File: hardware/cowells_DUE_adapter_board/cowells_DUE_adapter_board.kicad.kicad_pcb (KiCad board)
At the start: 2 copper layers, 123.8 x 53.3 mm, 41 parts, among them J1 DRV8305J1, J2 DRV8305J2, J3 AS5048A, J4 spindl enc., J5 AS5311AB, J6 AS5311AB, SW1 Run, SW2 Dir, SW3 eStop, SW4 sw_rst, SW5 SW_DIP_x03, U1 NL17SZ14, Y1 20MHz

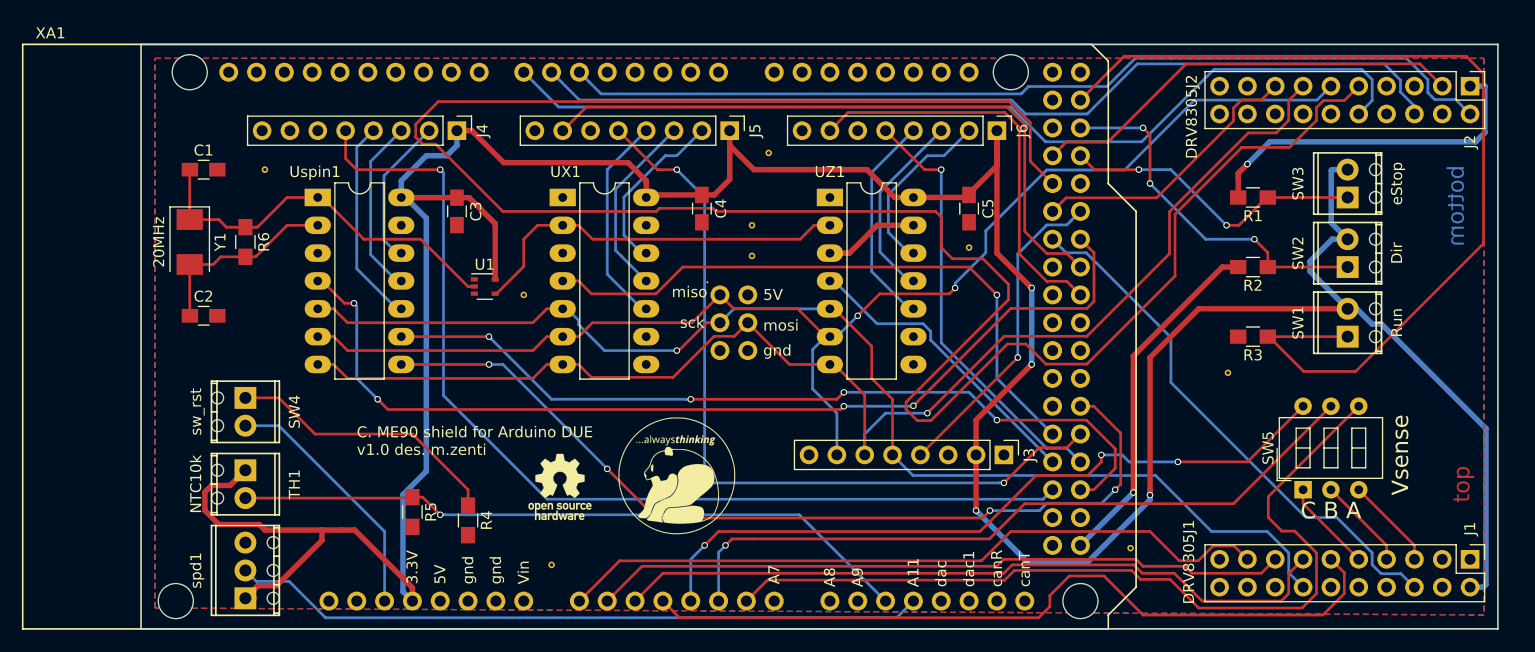
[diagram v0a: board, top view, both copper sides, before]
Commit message: cleanup of old code
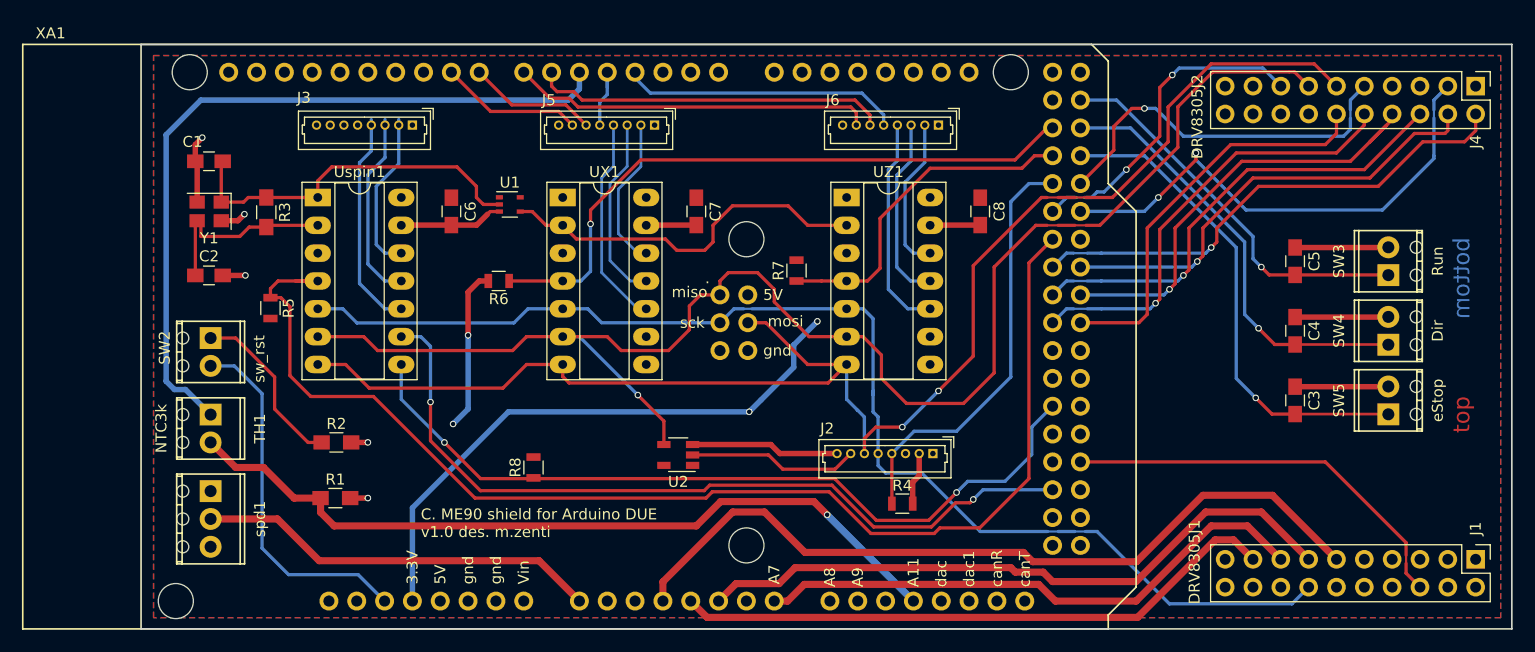
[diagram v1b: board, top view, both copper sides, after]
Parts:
- removed G***: LOGO, customSymbols:alwaysthinking_logo_10.8x10.8mm
- removed the J4 at (131.1, 70.1)
- removed the R1 at (203.7, 76.2)
- removed the R2 at (203.7, 82.5)
- removed the R3 at (203.7, 88.9)
- removed REF** (x9): stitching_VIA_0.6mm, customSymbols:stitching_VIA_0.6mm
- removed REF***: OSHW-Logo_5.7x6mm_SilkScreen, Symbols:OSHW-Logo_5.7x6mm_SilkScreen
- removed SW1: Run, TerminalBlocks_Phoenix:TerminalBlock_Phoenix_MPT-2.54mm_2pol
- removed the SW5 at (208.3, 102.9)
- added C3: 15n, Capacitors_SMD:C_0805_HandSoldering, F.Cu at (207.6, 94.7)
- added C4: 15n, Capacitors_SMD:C_0805_HandSoldering, F.Cu at (207.6, 88.4)
- added C5: 15n, Capacitors_SMD:C_0805_HandSoldering, F.Cu at (207.6, 82.0)
- added J2: AS5048A, Connectors_Molex:Molex_PicoBlade_53047-0810_08x1.25mm_Straight, F.Cu at (174.5, 99.6)
- added R4: 10k, Resistors_SMD:R_0805, F.Cu at (171.7, 104.1)
- added R5: 10k, Resistors_SMD:R_0805, F.Cu at (114.0, 86.3)
- added R6: 10k, Resistors_SMD:R_0805, F.Cu at (134.9, 83.8)
- added R7: 10k, Resistors_SMD:R_0805, F.Cu at (162.1, 82.9)
- added R8: 10k, Resistors_SMD:R_0805, F.Cu at (138.0, 100.8)
- added SW3: Run, TerminalBlocks_Phoenix:TerminalBlock_Phoenix_MPT-2.54mm_2pol, F.Cu at (216.1, 83.3)
- added U2: 74AHC1G125, TO_SOT_Packages_SMD:TSOT-23-5, F.Cu at (151.3, 99.7)
- C1, C2: value Cm -> 18p
- J3: value AS5048A -> spindl enc.; footprint Pin_Headers:Pin_Header_Straight_1x08_Pitch2.54mm -> Connectors_Molex:Molex_PicoBlade_53047-0810_08x1.25mm_Straight
- J5, J6: footprint Pin_Headers:Pin_Header_Straight_1x08_Pitch2.54mm -> Connectors_Molex:Molex_PicoBlade_53047-0810_08x1.25mm_Straight
- R1: renamed from R5; value 5k -> 1k
- TH1: value NTC10k -> NTC3k
- UX1, UZ1, Uspin1: footprint Housings_DIP:DIP-14_W7.62mm_LongPads -> Housings_DIP:DIP-14_W7.62mm_Socket_LongPads
- XA1: footprint Arduino:Arduino_Due_Shield_noHoles -> customFootPrints:Arduino_Due_Shield_drv8305
- Y1: value 20MHz -> 10MHz; footprint Crystals:Crystal_SMD_Abracon_ABM3-2pin_5.0x3.2mm -> Crystals:Crystal_SMD_3225-4pin_3.2x2.5mm
- spd1: value 0.3k -> 5k
- moved J3 61.8 mm to (127.0, 69.6), turned to 180 degrees
- moved SW5 20.1 mm to (216.1, 96.0)
- moved R2 14.0 mm to (120.1, 98.6), turned to 0 degrees
- moved spd1 10.3 mm to (108.6, 103.0), turned to 270 degrees
- moved SW4 8.00 mm to (216.1, 89.6)
- moved U1 7.83 mm to (135.9, 76.8)
- moved R1 7.15 mm to (120.0, 103.6), turned to 0 degrees
- moved J5 6.88 mm to (149.1, 69.6), turned to 180 degrees
- moved SW2 6.32 mm to (108.6, 89.0)
- moved TH1 5.99 mm to (108.6, 96.0)
- moved J6 5.36 mm to (175.0, 69.6), turned to 180 degrees
- moved C2 3.72 mm to (108.4, 83.3)
- moved R3 3.32 mm to (113.7, 77.5)
- moved Y1 3.31 mm to (108.5, 77.5), turned to 180 degrees
- moved UZ1 1.52 mm to (166.6, 76.2)
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- renumbered C3 to C6, C4 to C7, C5 to C8, J2 to J4, R4 to R2, R6 to R3, SW4 to SW2, SW2 to SW4, SW3 to SW5
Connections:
- J1 pad 14: /SCLK -> /SCK
- J1 pad 2: VCC -> Net-(J1-Pad2)
- J1 pad 5: Net-(J1-Pad5) -> /VsenA
- J1 pad 7: Net-(J1-Pad7) -> /VsenB
- J1 pad 9: Net-(J1-Pad9) -> /VsenC
- J3 pad 1: /5v -> VCC
- J3 pad 2: VCC -> Net-(J3-Pad2)
- J3 pad 3: /PWM -> Net-(J3-Pad3)
- J3 pad 4: /CsnMot -> Net-(J3-Pad4)
- J3 pad 5: /SCLK -> Net-(J3-Pad5)
- J3 pad 6: /SDO -> GND
- J3 pad 7: /SDI -> Net-(J3-Pad7)
- J4 pad 11: /SDI -> /MOSI
- J4 pad 13: /SDO -> /MISO
- J5 pad 6: GND -> /ClkX
- J5 pad 7: /PWMx -> /DoX
- J6 pad 6: GND -> /ClkZ
- J6 pad 7: /PWMz -> /DoZ
- SW4 pad 2: VCC -> GND
- SW5 pad 2: VCC -> GND
- TH1 pad 1: VCC -> /Th1Ex
- UX1 pad 5: /SCLK -> /SCK
- UX1 pad 6: /SDI -> /MISO
- UX1 pad 7: /SDO -> /MOSI
- UZ1 pad 5: /SCLK -> /SCK
- UZ1 pad 6: /SDI -> /MISO
- UZ1 pad 7: /SDO -> /MOSI
- Uspin1 pad 10: Net-(J4-Pad4) -> Net-(J3-Pad4)
- Uspin1 pad 11: Net-(J4-Pad3) -> Net-(J3-Pad3)
- Uspin1 pad 12: Net-(J4-Pad2) -> Net-(J3-Pad2)
- Uspin1 pad 5: /SCLK -> /SCK
- Uspin1 pad 6: /SDI -> /MISO
- Uspin1 pad 7: /SDO -> /MOSI
- XA1 pad A0: /IsenC -> /speed
- XA1 pad A1: /IsenB -> Net-(XA1-PadA1)
- XA1 pad A10: /TH1 -> Net-(XA1-PadA10)
- XA1 pad A11: Net-(XA1-PadA11) -> /TH1
- XA1 pad A2: /IsenA -> Net-(XA1-PadA2)
- XA1 pad A4: /VsenC -> /IsenC
- XA1 pad A5: /VsenB -> /IsenA
- XA1 pad A6: /VsenA -> Net-(XA1-PadA6)
- XA1 pad A7: Net-(XA1-PadA7) -> /IsenB
- XA1 pad D24: Net-(XA1-PadD24) -> /SS_x
- XA1 pad D26: /SCS -> /SS_z
- XA1 pad D28: /PWRGD -> /CsnMot
- XA1 pad D29: Net-(XA1-PadD29) -> /PWRGD
- XA1 pad D3: Net-(XA1-PadD3) -> /CsnZ
- XA1 pad D31: /CsnMot -> /SCS
- XA1 pad D32: /nFAULT -> /SS_spin
- XA1 pad D33: /SS_spin -> Net-(XA1-PadD33)
- XA1 pad D34: Net-(XA1-PadD34) -> /InH_A
- XA1 pad D35: /PWMx -> /InL_A
- XA1 pad D36: Net-(XA1-PadD36) -> /InH_B
- XA1 pad D37: /PWMz -> /InL_B
- XA1 pad D38: Net-(XA1-PadD38) -> /InH_C
- XA1 pad D39: Net-(XA1-PadD39) -> /InL_C
- XA1 pad D4: Net-(XA1-PadD4) -> /CsnX
- XA1 pad D44: Net-(XA1-PadD44) -> /SpnLFLAG
- XA1 pad D45: /SpnLFLAG -> Net-(XA1-PadD45)
- XA1 pad D46: /SS_x -> Net-(XA1-PadD46)
- XA1 pad D47: /CsnX -> Net-(XA1-PadD47)
- XA1 pad D48: /SS_z -> Net-(XA1-PadD48)
- XA1 pad D49: /CsnZ -> /nFAULT
- XA1 pad D5: /InH_A -> /Th1Ex
- XA1 pad D50: /CsnSpn -> /SpnDFLAG
- XA1 pad D51: /SpnDFLAG -> Net-(XA1-PadD51)
- XA1 pad D6: /InH_B -> /ClkZ
- XA1 pad D7: /InH_C -> /DoZ
- XA1 pad D8: Net-(XA1-PadD8) -> /ClkX
- XA1 pad D9: Net-(XA1-PadD9) -> /DoX
- XA1 pad MISO: /SDI -> /MISO
- XA1 pad MOSI: /SDO -> /MOSI
- XA1 pad SCK: /SCLK -> /SCK
- Y1 pad 2: Net-(C2-Pad1) -> GND
- spd1 pad 2: Net-(XA1-PadA11) -> /speed
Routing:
- net VCC: track 311.2 -> 73.4 mm
- net /PWRGD: track 202.0 -> 34.5 mm, vias 0 -> 1
- net /MISO: track 0.00 -> 139.7 mm, vias 0 -> 1
- net /MOSI: track 0.00 -> 137.7 mm, vias 0 -> 2
- net /SDI: track 120.1 -> 0.00 mm, vias 2 -> 0
- net /SDO: track 120.1 -> 0.00 mm, vias 1 -> 0
- net /SCK: track 0.00 -> 113.9 mm
- net /SCLK: track 110.6 -> 0.00 mm, vias 1 -> 0
- net /CsnSpn: track 92.2 -> 0.00 mm, vias 1 -> 0
- net /VsenA: track 78.8 -> 0.00 mm
- net /Th1Ex: track 0.00 -> 68.8 mm
- net /VsenC: track 66.4 -> 0.00 mm, vias 3 -> 0
- net /VsenB: track 65.8 -> 0.00 mm, vias 1 -> 0
- net /CsnX: track 72.2 -> 6.51 mm, vias 2 -> 0
- net Net-(XA1-PadA11): track 63.4 -> 0.00 mm
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- added copper zone on F.Cu, net VCC
- removed copper zone on F.Cu, net GND
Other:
- board size 123.8 x 53.3 mm -> 125.1 x 53.3 mm
- net class Default: clearance 0.25 -> 0.3; trace_width 0.25 -> 0.3
- net class PWM added: clearance 0.3, trace_width 0.3, via_dia 0.6, via_drill 0.4
- net class sensitive added: clearance 0.3, trace_width 0.65, via_dia 0.6, via_drill 0.4
- rule trace_clearance: 0.25 -> 0.3
- board text added: "Due Edge"
- board text added: "Due power Connector"
- board text removed: "C B A"
- board text removed: "Vsense"
